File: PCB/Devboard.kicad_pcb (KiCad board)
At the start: 2 copper layers, 21 x 51 mm, 33 parts, among them J4 Conn_01x03

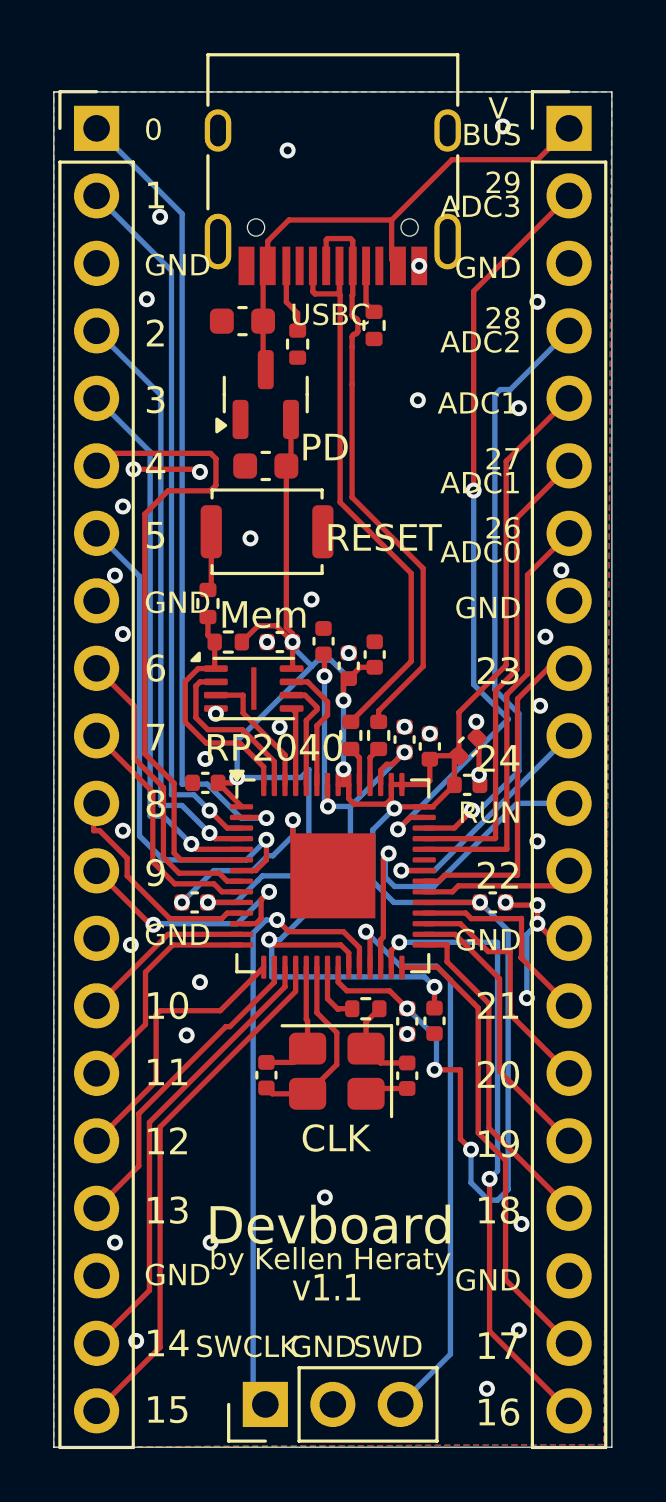
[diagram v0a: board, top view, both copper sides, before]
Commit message: added LEDs
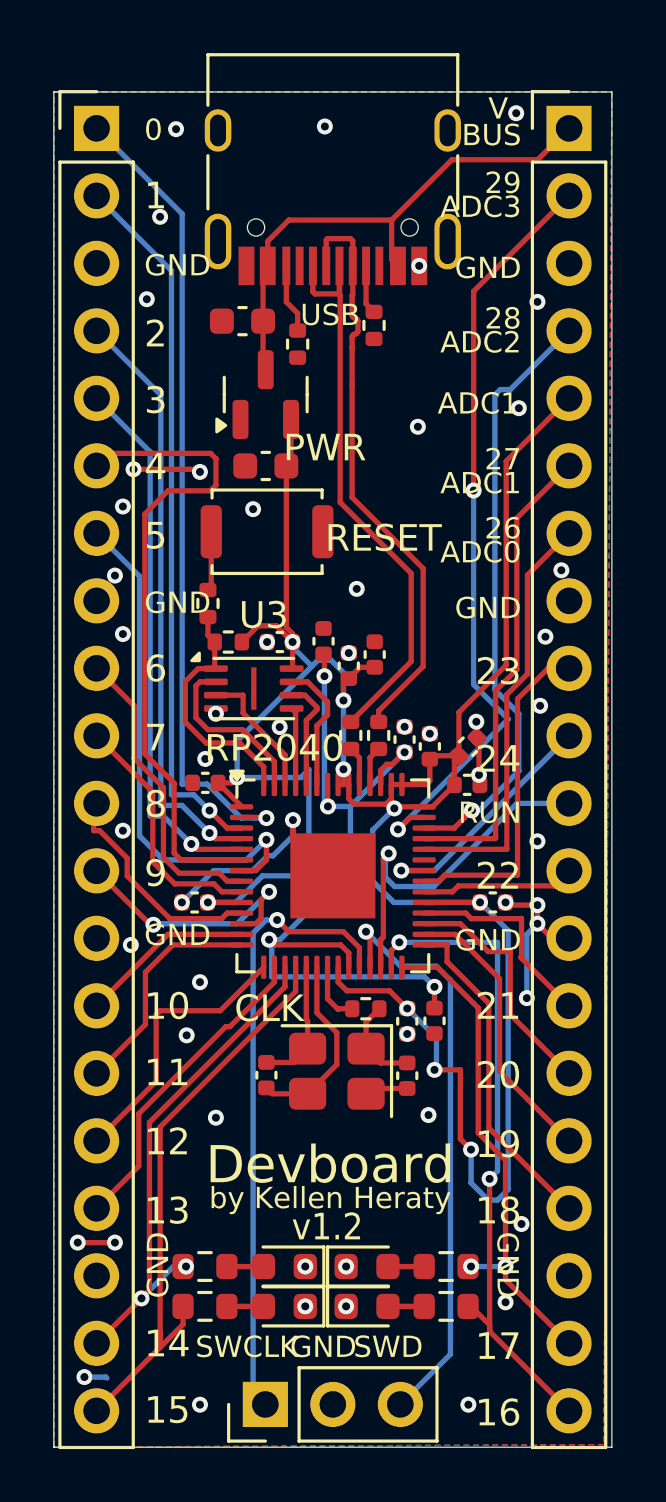
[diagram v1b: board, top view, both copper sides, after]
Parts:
- added D1: LED, LED_SMD:LED_0603_1608Metric, F.Cu at (98.2, 68.7)
- added D2: LED, LED_SMD:LED_0603_1608Metric, F.Cu at (98.2, 70.2)
- added D3: LED, LED_SMD:LED_0603_1608Metric, F.Cu at (101.3, 70.2)
- added D4: LED, LED_SMD:LED_0603_1608Metric, F.Cu at (101.3, 68.7)
- added R10: 330, Resistor_SMD:R_0603_1608Metric, F.Cu at (104.3, 70.2)
- added R11: 330, Resistor_SMD:R_0603_1608Metric, F.Cu at (104.3, 68.7)
- added R8: 330, Resistor_SMD:R_0603_1608Metric, F.Cu at (95.2, 68.7)
- added R9: 330, Resistor_SMD:R_0603_1608Metric, F.Cu at (95.2, 70.2)
- renumbered L to J2, R to J3, PD to PWR, Mem to U3, USBC to USB
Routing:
- net GPIO15: track 19.8 -> 22.1 mm
- net GPIO14: track 17.1 -> 19.4 mm, vias 0 -> 2
- net GND: track 26.5 -> 28.7 mm, vias 46 -> 53
- net GPIO17: track 17.9 -> 19.4 mm, vias 0 -> 2
- net Net-(D2-A): track 0.00 -> 1.38 mm
- net Net-(D1-A): track 0.00 -> 1.38 mm
- net Net-(D3-A): track 0.00 -> 1.36 mm
- net Net-(D4-A): track 0.00 -> 1.36 mm
- net GPIO16: track 23.7 -> 25.1 mm
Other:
- board text added: "v1.2"
- board text removed: "v1.1"
